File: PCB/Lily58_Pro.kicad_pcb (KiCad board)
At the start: 2 copper layers, 142.5 x 106.3 mm, 85 parts, among them J1 LED, J2 4PIN, J3 OLED, P1 i2c_pin, P2 i2c_pin, SW1 SW_PUSH, SW10 SW_PUSH, SW11 SW_PUSH, SW12 SW_PUSH, SW13 SW_PUSH, SW14 SW_PUSH, SW15 SW_PUSH, SW16 SW_PUSH, SW17 SW_PUSH, SW18 SW_PUSH, SW19 SW_PUSH, SW2 SW_PUSH, SW20 SW_PUSH, SW21 SW_PUSH, SW22 SW_PUSH, SW23 SW_PUSH, SW24 SW_PUSH, SW25 SW_PUSH, SW26 SW_PUSH, SW27 SW_PUSH, SW28 SW_PUSH, SW29 SW_PUSH, SW3 SW_PUSH, SW4 SW_PUSH, SW5 SW_PUSH, SW6 SW_PUSH, SW7 SW_PUSH, SW8 SW_PUSH, SW9 SW_PUSH, U1 ProMicro

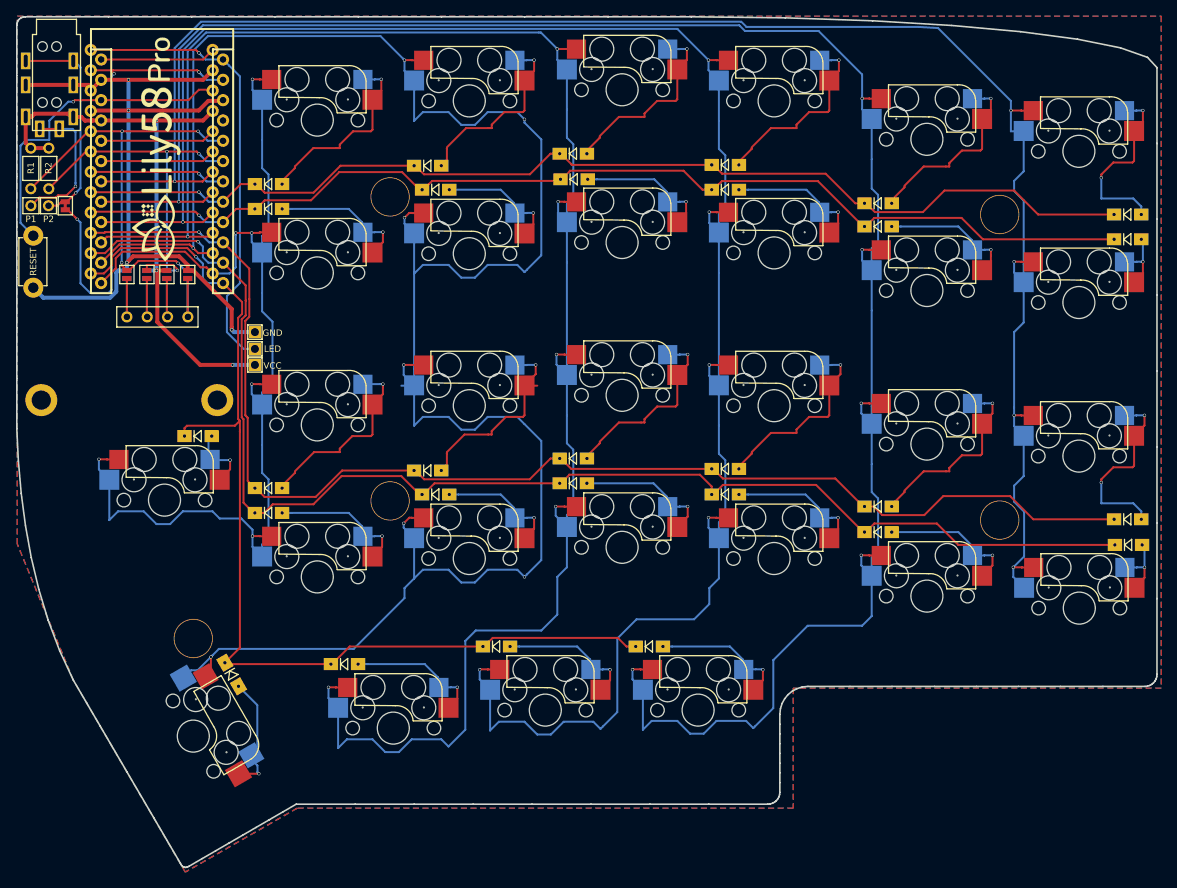
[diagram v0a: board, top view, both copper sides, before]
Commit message: Fix switch drill holes
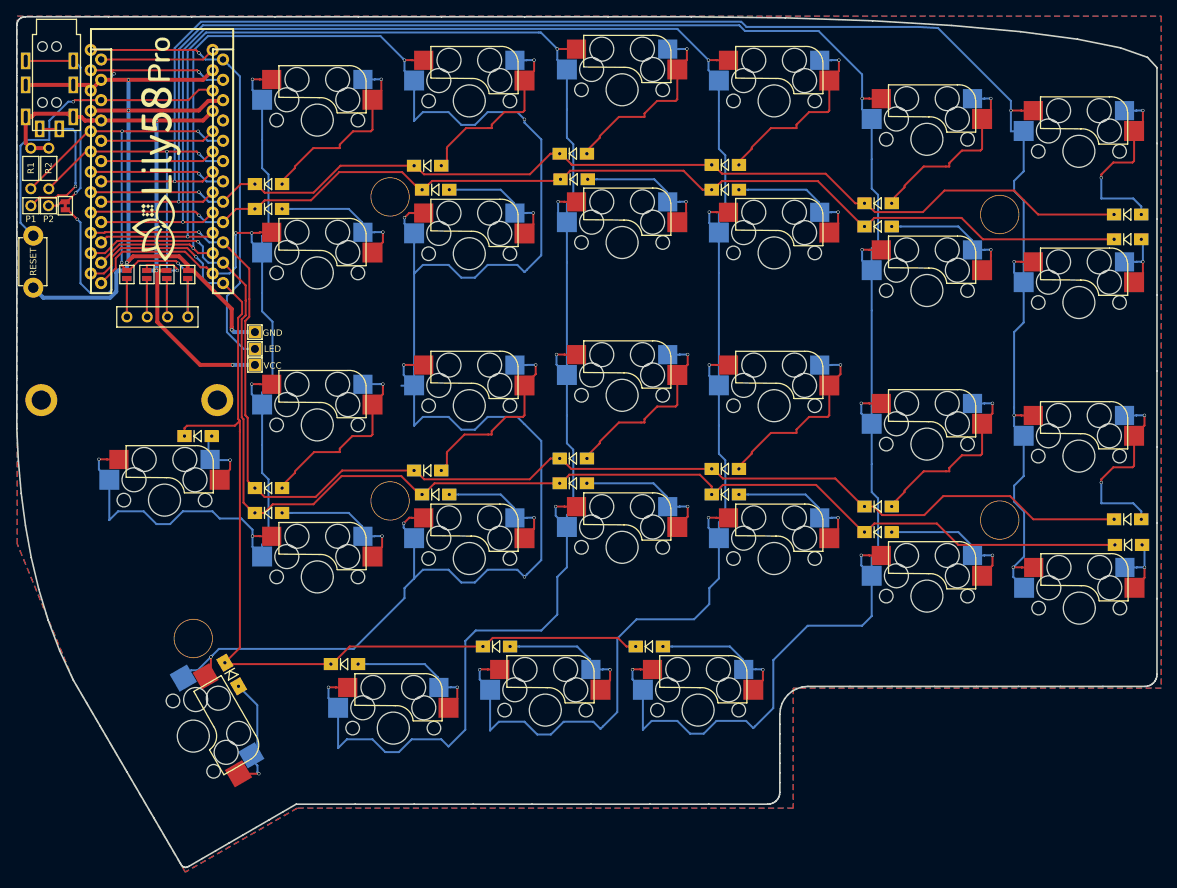
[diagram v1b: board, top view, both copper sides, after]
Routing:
- net Net-(D14-Pad2): track 25.6 -> 24.1 mm

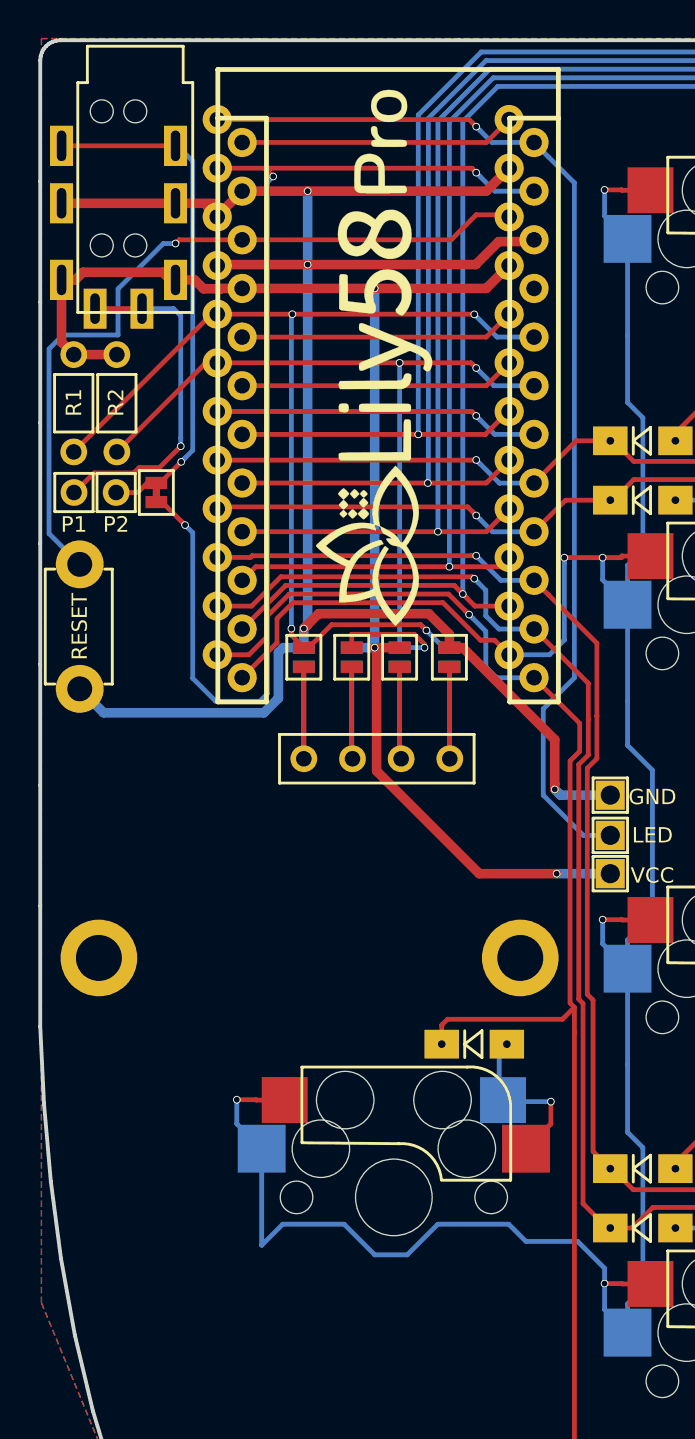
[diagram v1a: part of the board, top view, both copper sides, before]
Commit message: Add rotary encoder
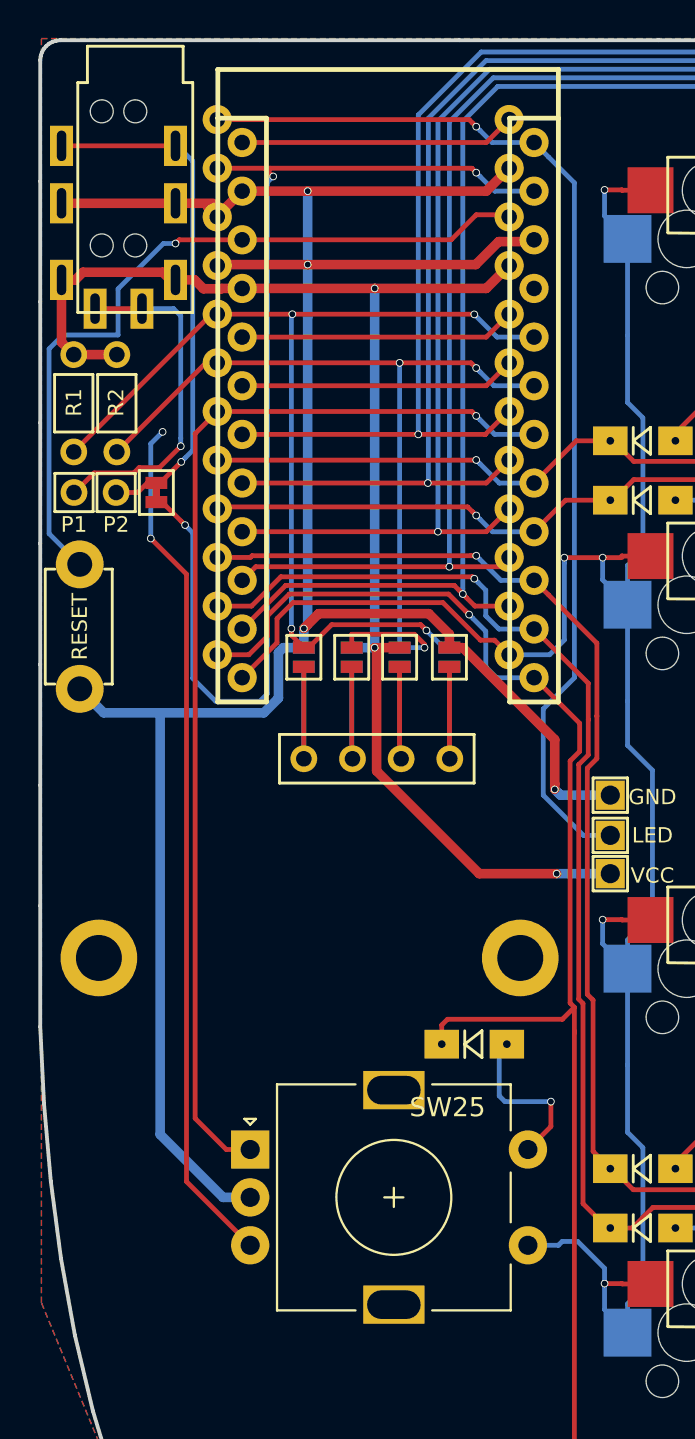
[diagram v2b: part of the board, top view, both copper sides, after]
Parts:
- removed G*** (x2): LOGO, Lily58-footprint:lily58_logo_Pro
- JP1, JP2, JP3, JP4, JP5, JP6, JP7, JP8: value (none) -> Jumper_NO_Small
- SW25: value SW_PUSH -> Rotary_Encoder_Switch; footprint fractory:MX_Choc_Hotswap -> fractory:RotaryEncoder_Alps_EC11E-Switch_Vertical_H20mm
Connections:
- U1 pad 19: Net-(U1-Pad19) -> enc2
- U1 pad 7: Net-(U1-Pad7) -> enc1
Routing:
- net enc2: track 0.00 -> 59.3 mm, vias 0 -> 2
- net enc1: track 0.00 -> 58.0 mm, vias 0 -> 1
- net GND: track 103.0 -> 131.1 mm
- net col5: track 141.3 -> 114.6 mm, vias 6 -> 5
- net Net-(U1-Pad7): track 17.0 -> 0.00 mm, vias 1 -> 0
- net Net-(U1-Pad19): track 14.4 -> 0.00 mm

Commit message: WIP underglow/backlight
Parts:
- added L1: SK6812mini, fractory:SK6812MINI, F.Cu at (120.5, 54.5)
- added L10: SK6812mini, fractory:SK6812MINI, F.Cu at (177.6, 71.1)
- added L11: SK6812mini, fractory:SK6812MINI, F.Cu at (196.7, 75.8)
- added L12: SK6812mini, fractory:SK6812MINI, F.Cu at (215.7, 77.3)
- added L13: SK6812mini, fractory:SK6812MINI, F.Cu at (120.5, 92.6)
- added L14: SK6812mini, fractory:SK6812MINI, F.Cu at (139.5, 90.2)
- added L15: SK6812mini, fractory:SK6812MINI, F.Cu at (158.6, 88.9)
- added L16: SK6812mini, fractory:SK6812MINI, F.Cu at (177.6, 90.2)
- added L17: SK6812mini, fractory:SK6812MINI, F.Cu at (196.7, 95.0)
- added L18: SK6812mini, fractory:SK6812MINI, F.Cu at (215.7, 96.5)
- added L19: SK6812mini, fractory:SK6812MINI, F.Cu at (120.5, 111.6)
- added L2: SK6812mini, fractory:SK6812MINI, F.Cu at (139.5, 52.1)
- added L20: SK6812mini, fractory:SK6812MINI, F.Cu at (139.5, 109.3)
- added L21: SK6812mini, fractory:SK6812MINI, F.Cu at (158.6, 107.9)
- added L22: SK6812mini, fractory:SK6812MINI, F.Cu at (177.6, 109.3)
- added L23: SK6812mini, fractory:SK6812MINI, F.Cu at (196.7, 114.0)
- added L24: SK6812mini, fractory:SK6812MINI, F.Cu at (215.8, 115.5)
- added L26: SK6812mini, fractory:SK6812MINI, F.Cu at (101.1, 129.2)
- added L27: SK6812mini, fractory:SK6812MINI, F.Cu at (130.0, 130.5)
- added L28: SK6812mini, fractory:SK6812MINI, F.Cu at (149.0, 128.2)
- added L29: SK6812mini, fractory:SK6812MINI, F.Cu at (168.1, 128.2)
- added L3: SK6812mini, fractory:SK6812MINI, F.Cu at (158.6, 50.7)
- added L30: SK6812mini, fractory:SK6812MINI_underglow, F.Cu at (122.2, 59.4)
- added L31: SK6812mini, fractory:SK6812MINI_underglow, F.Cu at (163.1, 55.3)
- added L32: SK6812mini, fractory:SK6812MINI_underglow, F.Cu at (198.6, 61.5)
- added L33: SK6812mini, fractory:SK6812MINI_underglow, F.Cu at (116.3, 118.7)
- added L34: SK6812mini, fractory:SK6812MINI_underglow, F.Cu at (154.1, 113.0)
- added L35: SK6812mini, fractory:SK6812MINI_underglow, F.Cu at (198.5, 99.8)
- added L4: SK6812mini, fractory:SK6812MINI, F.Cu at (177.6, 52.1)
- added L5: SK6812mini, fractory:SK6812MINI, F.Cu at (196.7, 56.9)
- added L6: SK6812mini, fractory:SK6812MINI, F.Cu at (215.7, 58.4)
- added L7: SK6812mini, fractory:SK6812MINI, F.Cu at (120.5, 73.6)
- added L8: SK6812mini, fractory:SK6812MINI, F.Cu at (139.5, 71.2)
- added L9: SK6812mini, fractory:SK6812MINI, F.Cu at (158.6, 69.8)

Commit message: WIP underglow/backlight
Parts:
- added L25: SK6812mini, fractory:SK6812MINI, F.Cu at (97.6, 107.6)
- W1: footprint Lily58-footprint:jumper_data -> fractory:SolderJumper-2_P1.3mm_Bridged_Pad1.0x1.5mm
- moved J1 41.9 mm to (118.1, 39.5), turned to 90 degrees
- moved D22 22.2 mm to (187.2, 112.6), turned to 90 degrees
- moved D10 21.8 mm to (187.2, 73.8), turned to 90 degrees
- moved D9 20.3 mm to (168.2, 70.3), turned to 90 degrees
- moved D11 20.2 mm to (206.2, 76.1), turned to 90 degrees
- moved D19 20.1 mm to (130.1, 111.6), turned to 90 degrees
- moved D23 19.9 mm to (206.3, 113.8), turned to 90 degrees
- moved D21 19.9 mm to (168.1, 107.8), turned to 90 degrees
- moved D28 19.3 mm to (158.5, 127.2), turned to 90 degrees
- moved D27 19.3 mm to (139.6, 129.2), turned to 90 degrees
- moved D7 18.9 mm to (130.0, 71.8), turned to 90 degrees
- moved D18 17.7 mm to (215.8, 83.3)
- moved D20 17.7 mm to (149.1, 107.8), turned to 90 degrees
- moved D8 17.5 mm to (149.1, 69.4), turned to 90 degrees
- moved D1 16.4 mm to (130.0, 52.8), turned to 90 degrees
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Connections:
- L26 pad 3: Net-(L19-Pad1) -> Net-(L25-Pad1)
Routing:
- net VCC: track 72.9 -> 957.2 mm, vias 3 -> 22
- net GND: track 131.1 -> 0.00 mm, vias 4 -> 0
- net col4: track 269.2 -> 177.3 mm, vias 8 -> 5
- net Net-(L34-Pad1): track 0.00 -> 58.5 mm, vias 0 -> 3
- net LED: track 57.0 -> 114.2 mm, vias 1 -> 2
- net Net-(L33-Pad1): track 0.00 -> 51.1 mm, vias 0 -> 2
- net Net-(L32-Pad3): track 0.00 -> 51.1 mm, vias 0 -> 2
- net col1: track 262.8 -> 214.0 mm
- net col2: track 246.5 -> 199.3 mm
- net Net-(L31-Pad3): track 0.00 -> 44.7 mm, vias 0 -> 2
- net Net-(L30-Pad3): track 0.00 -> 42.0 mm, vias 0 -> 2
- net Net-(L5-Pad1): track 0.00 -> 40.1 mm, vias 0 -> 2
- net Net-(L26-Pad1): track 0.00 -> 38.8 mm, vias 0 -> 2
- net Net-(L1-Pad1): track 0.00 -> 34.8 mm, vias 0 -> 2
- net Net-(L2-Pad1): track 0.00 -> 33.6 mm, vias 0 -> 3
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
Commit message: Finishing underglow/backlight
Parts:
- SW25: footprint fractory:RotaryEncoder_Alps_EC11E-Switch_Vertical_H20mm -> fractory:RotaryEncoder_optional
- moved L25 7.01 mm to (101.4, 101.8), turned to 180 degrees
- turned L26 to 210 degrees
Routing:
- net VCC: track 957.2 -> 0.00 mm, vias 22 -> 0
- net col1: track 214.0 -> 0.00 mm, vias 6 -> 0
- net col0: track 209.1 -> 0.00 mm, vias 4 -> 0
- net col3: track 200.8 -> 0.00 mm, vias 6 -> 0
- net col2: track 199.3 -> 0.00 mm, vias 6 -> 0
- net row3: track 179.4 -> 0.00 mm, vias 1 -> 0
- net col4: track 177.3 -> 0.00 mm, vias 5 -> 0
- net row2: track 165.6 -> 0.00 mm, vias 3 -> 0
- net row1: track 157.3 -> 0.00 mm, vias 3 -> 0
- net row4: track 149.8 -> 0.00 mm
- net row0: track 129.4 -> 0.00 mm
- net LED: track 114.2 -> 0.00 mm, vias 2 -> 0
- net col5: track 99.5 -> 0.00 mm, vias 4 -> 0
- net enc2: track 62.7 -> 0.00 mm, vias 1 -> 0
- net Net-(L34-Pad1): track 58.5 -> 0.00 mm, vias 3 -> 0
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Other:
- outline, holes or cut-outs redrawn

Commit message: WIP net
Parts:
- turned L25 to 0 degrees
- turned L26 to 300 degrees
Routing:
- net VCC: track 0.00 -> 203.9 mm, vias 0 -> 35
- net GND: track 0.00 -> 188.0 mm, vias 0 -> 35
- net Net-(L31-Pad3): track 0.00 -> 7.83 mm, vias 0 -> 2
- net Net-(L34-Pad1): track 0.00 -> 7.81 mm, vias 0 -> 2
- net Net-(L30-Pad3): track 0.00 -> 7.73 mm, vias 0 -> 2
- net Net-(L32-Pad3): track 0.00 -> 7.59 mm, vias 0 -> 2
- net Net-(L1-Pad3): track 0.00 -> 7.51 mm, vias 0 -> 2
- net Net-(L21-Pad3): track 0.00 -> 7.44 mm, vias 0 -> 2
- net Net-(L33-Pad1): track 0.00 -> 7.41 mm, vias 0 -> 2
- net Net-(L28-Pad1): track 0.00 -> 7.38 mm, vias 0 -> 2
- net Net-(L25-Pad1): track 0.00 -> 7.34 mm, vias 0 -> 2
- net Net-(L18-Pad1): track 0.00 -> 7.31 mm, vias 0 -> 2
- net Net-(L26-Pad1): track 0.00 -> 7.27 mm, vias 0 -> 2
- net Net-(L19-Pad3): track 0.00 -> 7.25 mm, vias 0 -> 2
- net Net-(L3-Pad1): track 0.00 -> 7.15 mm, vias 0 -> 2
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
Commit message: WIP net
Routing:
- net col2: track 0.00 -> 26.0 mm, vias 0 -> 5
- net col3: track 0.00 -> 25.9 mm, vias 0 -> 5
- net col4: track 0.00 -> 23.9 mm, vias 0 -> 5
- net col1: track 0.00 -> 20.8 mm, vias 0 -> 4
- net col5: track 0.00 -> 20.4 mm, vias 0 -> 4
- net col0: track 0.00 -> 20.0 mm, vias 0 -> 4
- net (no net): track 0.00 -> 10.2 mm, vias 0 -> 2
- net Net-(D29-Pad2): track 0.00 -> 5.40 mm, vias 0 -> 1
- net Net-(D28-Pad2): track 0.00 -> 5.33 mm, vias 0 -> 1
- net Net-(D9-Pad2): track 0.00 -> 5.31 mm, vias 0 -> 1
- net Net-(D5-Pad2): track 0.00 -> 5.29 mm, vias 0 -> 1
- net Net-(D16-Pad2): track 0.00 -> 5.25 mm, vias 0 -> 1
- net Net-(D12-Pad2): track 0.00 -> 5.25 mm, vias 0 -> 1
- net Net-(D20-Pad2): track 0.00 -> 5.22 mm, vias 0 -> 1
- net Net-(D13-Pad2): track 0.00 -> 5.21 mm, vias 0 -> 1
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
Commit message: WIP net
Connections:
- D25 pad 2: Net-(D25-Pad2) -> (no net)
- SW25 pad 1: (no net) -> col5
- SW25 pad 2: (no net) -> Net-(D25-Pad2)
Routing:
- net Net-(D25-Pad2): track 0.00 -> 20.6 mm, vias 0 -> 1
- net Net-(D6-Pad2): track 5.17 -> 25.2 mm
- net col5: track 20.4 -> 36.0 mm, vias 4 -> 5
- net Net-(D4-Pad2): track 5.15 -> 19.0 mm
- net Net-(D10-Pad2): track 5.15 -> 18.5 mm
- net Net-(D16-Pad2): track 5.25 -> 17.7 mm
- net Net-(D22-Pad2): track 5.19 -> 17.6 mm
- net Net-(D23-Pad2): track 1.80 -> 14.0 mm, vias 0 -> 1
- net Net-(D9-Pad2): track 5.31 -> 16.4 mm
- net Net-(D11-Pad2): track 5.11 -> 15.9 mm
- net Net-(D21-Pad2): track 5.11 -> 15.3 mm
- net (no net): track 10.2 -> 0.00 mm, vias 2 -> 0
- net Net-(D3-Pad2): track 5.15 -> 14.9 mm
- net Net-(D19-Pad2): track 4.92 -> 14.6 mm
- net Net-(D27-Pad2): track 5.14 -> 14.6 mm
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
